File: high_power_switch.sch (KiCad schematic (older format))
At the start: 3 parts

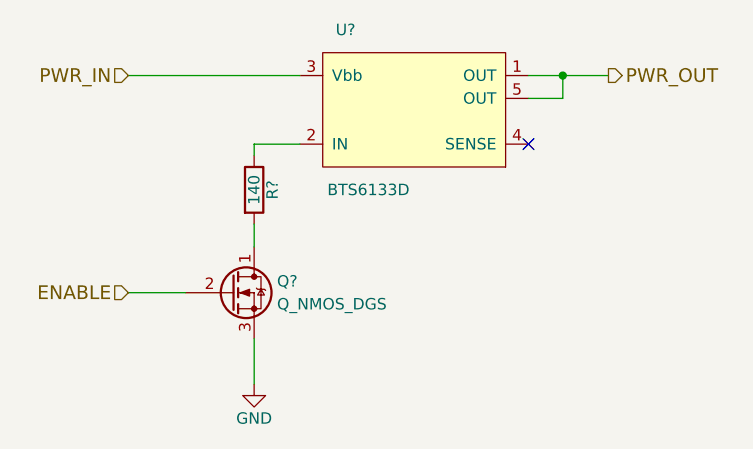
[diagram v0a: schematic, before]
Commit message: power switches connect to pgnd
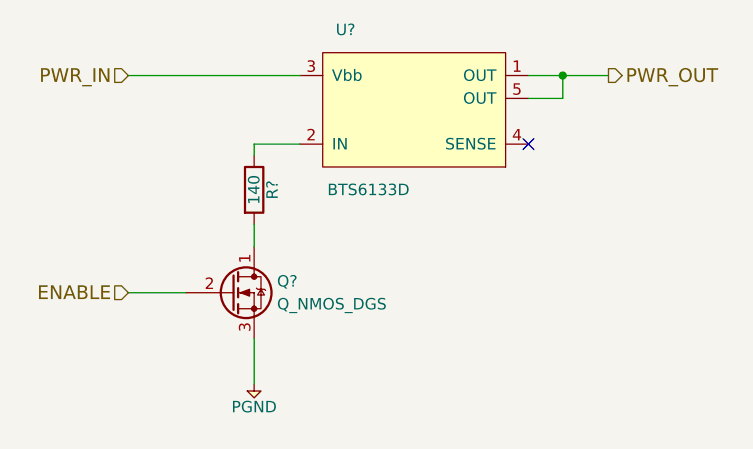
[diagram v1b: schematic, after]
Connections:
- net GND renamed PGND
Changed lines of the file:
@@
 Wire Wire Line
 	5100 3650 5300 3650
-$Comp
-L GND #PWR?
-U 1 1 59625B7B
-P 5100 4700
-F 0 "#PWR?" H 5100 4450 50  0001 C CNN
-F 1 "GND" H 5100 4550 50  0000 C CNN
-F 2 "" H 5100 4700 50  0001 C CNN
-F 3 "" H 5100 4700 50  0001 C CNN
-	1    5100 4700
-	1    0    0    -1
-$EndComp
 Wire Wire Line
 	5100 4700 5100 4500
@@
 Wire Wire Line
 	4550 4300 4800 4300
+$Comp
+L PGND #PWR?
+U 1 1 5962B512
+P 5100 4700
+F 0 "#PWR?" H 4970 4740 50  0001 L CNN
+F 1 "PGND" H 5100 4600 50  0000 C CNN
+F 2 "" H 5100 4700 60  0001 C CNN
+F 3 "" H 5100 4700 60  0001 C CNN
+	1    5100 4700
+	1    0    0    -1
+$EndComp
 $EndSCHEMATC

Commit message: more cleaning
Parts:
- R?: value 140 -> 100
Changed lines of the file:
@@
 $Descr A4 11693 8268
 encoding utf-8
-Sheet 7 8
+Sheet 8 9
 Title ""
 Date ""
@@
 U 1 1 596258EA
 P 5800 3450
+AR Path="/5957D255/596222E8/596258EA" Ref="U?"  Part="1"
+AR Path="/5957D255/596398D9/596258EA" Ref="U?"  Part="1"
 F 0 "U?" H 5500 3750 50  0000 C CNN
 F 1 "BTS6133D" H 5600 3050 50  0000 C CNN
@@
 U 1 1 59625A84
 P 5000 4300
+AR Path="/5957D255/596222E8/59625A84" Ref="Q?"  Part="1"
+AR Path="/5957D255/596398D9/59625A84" Ref="Q?"  Part="1"
 F 0 "Q?" H 5200 4350 50  0000 L CNN
 F 1 "Q_NMOS_DGS" H 5200 4250 50  0000 L CNN
@@
 U 1 1 59625AF9
 P 5100 3850
+AR Path="/5957D255/596222E8/59625AF9" Ref="R?"  Part="1"
+AR Path="/5957D255/596398D9/59625AF9" Ref="R?"  Part="1"
 F 0 "R?" V 5180 3850 50  0000 C CNN
-F 1 "140" V 5100 3850 50  0000 C CNN
+F 1 "100" V 5100 3850 50  0000 C CNN
 F 2 "" V 5030 3850 50  0001 C CNN
 F 3 "" H 5100 3850 50  0001 C CNN
@@
 U 1 1 5962B512
 P 5100 4700
+AR Path="/5957D255/596222E8/5962B512" Ref="#PWR?"  Part="1"
+AR Path="/5957D255/596398D9/5962B512" Ref="#PWR?"  Part="1"
 F 0 "#PWR?" H 4970 4740 50  0001 L CNN
 F 1 "PGND" H 5100 4600 50  0000 C CNN

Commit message: clean up after annotate
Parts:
- gave numbers to parts that had none: 3
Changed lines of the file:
@@
 P 5800 3450
 AR Path="/5957D255/596222E8/596258EA" Ref="U?"  Part="1"
-AR Path="/5957D255/596398D9/596258EA" Ref="U?"  Part="1"
-F 0 "U?" H 5500 3750 50  0000 C CNN
+AR Path="/5957D255/596398D9/596258EA" Ref="U6"  Part="1"
+F 0 "U6" H 5500 3750 50  0000 C CNN
 F 1 "BTS6133D" H 5600 3050 50  0000 C CNN
 F 2 "" H 6850 3050 50  0001 C CNN
@@
 P 5000 4300
 AR Path="/5957D255/596222E8/59625A84" Ref="Q?"  Part="1"
-AR Path="/5957D255/596398D9/59625A84" Ref="Q?"  Part="1"
-F 0 "Q?" H 5200 4350 50  0000 L CNN
+AR Path="/5957D255/596398D9/59625A84" Ref="Q5"  Part="1"
+F 0 "Q5" H 5200 4350 50  0000 L CNN
 F 1 "Q_NMOS_DGS" H 5200 4250 50  0000 L CNN
 F 2 "" H 5200 4400 50  0001 C CNN
@@
 P 5100 3850
 AR Path="/5957D255/596222E8/59625AF9" Ref="R?"  Part="1"
-AR Path="/5957D255/596398D9/59625AF9" Ref="R?"  Part="1"
-F 0 "R?" V 5180 3850 50  0000 C CNN
+AR Path="/5957D255/596398D9/59625AF9" Ref="R1"  Part="1"
+F 0 "R1" V 5180 3850 50  0000 C CNN
 F 1 "100" V 5100 3850 50  0000 C CNN
 F 2 "" V 5030 3850 50  0001 C CNN
@@
 P 5100 4700
 AR Path="/5957D255/596222E8/5962B512" Ref="#PWR?"  Part="1"
-AR Path="/5957D255/596398D9/5962B512" Ref="#PWR?"  Part="1"
-F 0 "#PWR?" H 4970 4740 50  0001 L CNN
+AR Path="/5957D255/596398D9/5962B512" Ref="#PWR20"  Part="1"
+F 0 "#PWR20" H 4970 4740 50  0001 L CNN
 F 1 "PGND" H 5100 4600 50  0000 C CNN
 F 2 "" H 5100 4700 60  0001 C CNN

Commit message: fix issue with incorrect symbol
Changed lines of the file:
@@
 	6450 3450 6450 3350
 Wire Wire Line
-	6300 3350 6450 3350
-Wire Wire Line
-	6450 3350 6650 3350
+	6300 3350 6650 3350
 Connection ~ 6450 3350
 Text HLabel 6650 3350 2    60   Output ~ 0
@@
 P 5100 4700
 AR Path="/5957D255/596222E8/5962B512" Ref="#PWR?"  Part="1"
-AR Path="/5957D255/596398D9/5962B512" Ref="#PWR16"  Part="1"
-F 0 "#PWR16" H 4970 4740 50  0001 L CNN
+AR Path="/5957D255/596398D9/5962B512" Ref="#PWR016"  Part="1"
+F 0 "#PWR016" H 4970 4740 50  0001 L CNN
 F 1 "PGND" H 5100 4600 50  0000 C CNN
 F 2 "" H 5100 4700 60  0001 C CNN
